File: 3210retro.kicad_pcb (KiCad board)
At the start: 6 copper layers, 44 x 118 mm, 196 parts, among them J1101 MICRO_SD_HINGE, J801 TEST_2P, P101 USB_OTG, P103 LIPO, P104 DC, P106 SPEAKER, P107 HEADPHONE, P108 RUMBLE, P301 SEPS525, P801 JTAG, Q501 MMBF170, Q701 MMBF170, SW701 SW_PUSH, SW702 C, SW703 1, SW704 4ghi, SW705 7pqrs, SW706 -, SW707 2abc, SW708 5jkl, SW709 8tuv, SW710 UP, SW711 3def, SW712 6mno, SW713 9wxyz, SW714 *+, SW715 DOWN, SW716 0space, SW717 #up, U1301 LSM9DS1, U201 MAX1555, U202 TPS62742, U203 TPS61021A, U301 TPS61041DBV, U401 TLV320ADC3101, U402 DRV8601, U403 TLV320DAC3100, U404 MP34DT01TR, U405 MP34DT01TR, U504 A7, U505 SIM_SLOT, U601 ESP-12E, U801 STM32F756VGTx, X101 ANT_GPS, X102 ANT_GSM, Y801 32kHz, Y802 24MHz

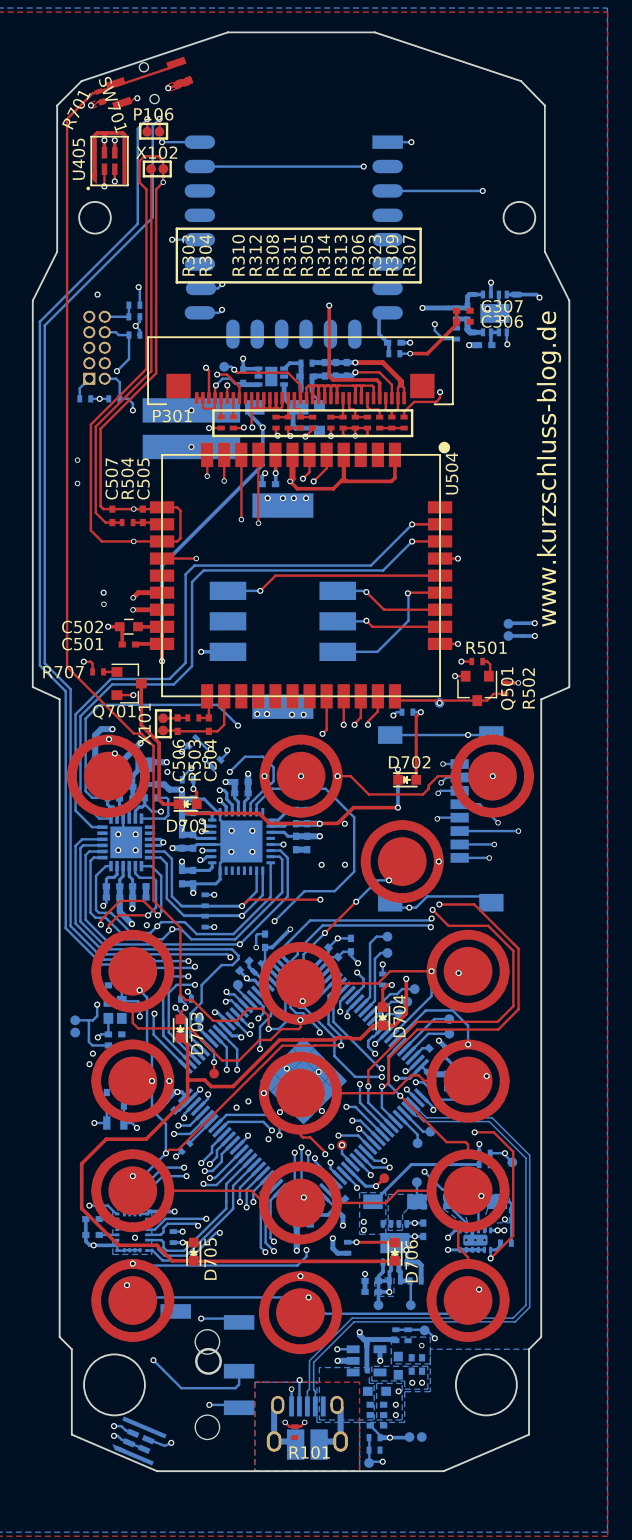
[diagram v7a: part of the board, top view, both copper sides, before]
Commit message: finalized borad further
placed more GND vias
make 4V_BST switchable
connect GND and GNDREF through resistor
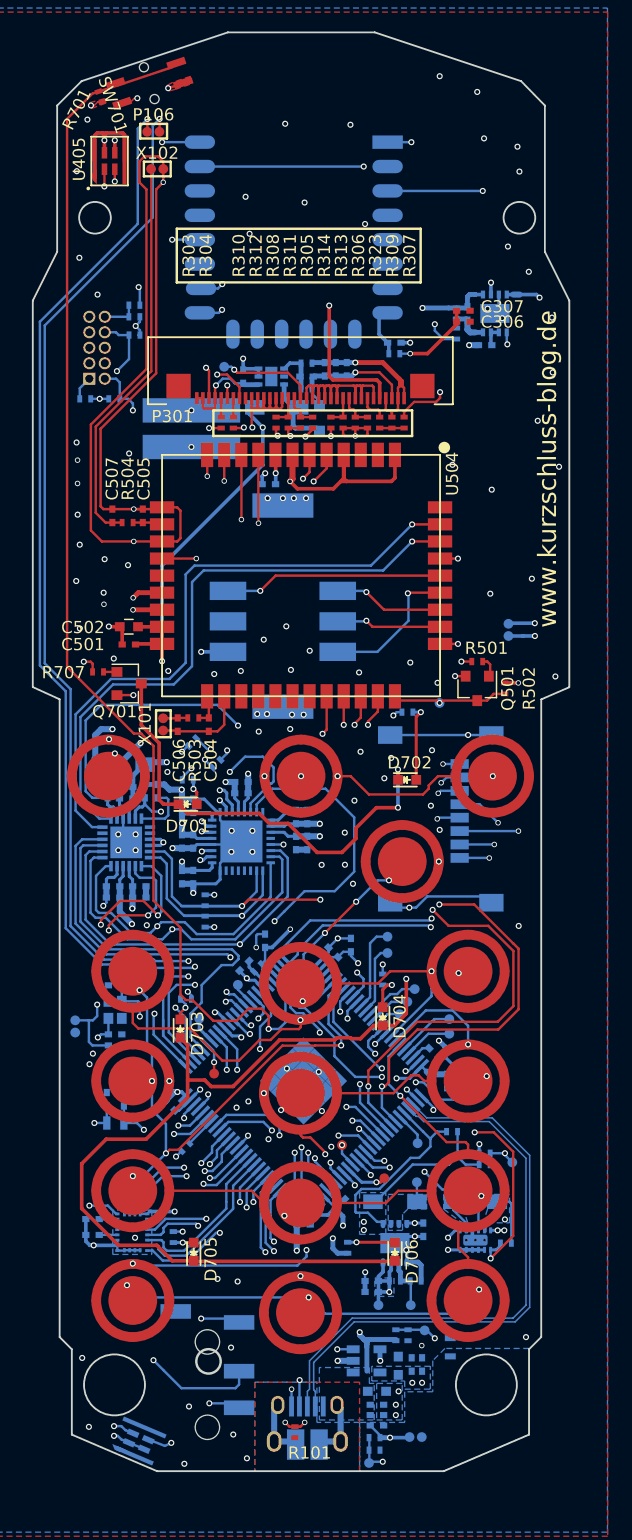
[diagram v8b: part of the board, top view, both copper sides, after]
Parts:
- removed TP113: TP, NokiaRetroFit:TP
- added R205: 10k, Resistors_SMD:R_0402_NoSilk, B.Cu at (111.8, 131.2)
- added R206: 0, Resistors_SMD:R_0603, B.Cu at (111.6, 148.9)
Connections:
- U203 pad 5: +BATT_LIPO -> /Controller/4V_BST_EN
- U401 pad 25: GNDA -> (no net)
- U403 pad 33: GNDA -> (no net)
- U801 pad 55: /Controller/PD8 -> /Controller/4V_BST_EN
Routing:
- net /Controller/4V_BST_EN: track 0.00 -> 17.0 mm
- net /Controller/PD8: track 2.77 -> 0.00 mm
- net +BATT_LIPO: track 83.3 -> 85.9 mm
- net Net-(D701-Pad1): track 120.3 -> 122.8 mm
- net +5V: track 40.4 -> 38.7 mm
- net /Buttons and LEDs/KEYPAD_COL1: track 44.1 -> 44.8 mm
- net /Radio Module, GPS and SIM/GPS_TX: track 65.8 -> 65.2 mm
- net /Controller/USB_ID: track 42.0 -> 41.5 mm
- net (no net): track 0.21 -> 0.00 mm, vias 1 -> 3
- net GND: track 199.9 -> 200.0 mm, vias 75 -> 141
- net GNDA: vias 16 -> 13
